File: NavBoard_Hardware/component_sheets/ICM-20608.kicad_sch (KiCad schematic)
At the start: 9 parts, among them U3 ICM-20608-G

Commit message: Updated sheet title info
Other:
- company: Missouri S&T Rover Design Team -> Thomas Francois, Katherine Dunlap, Missouri S&T Mars Rover Design Team
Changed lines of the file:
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@@
     (date "2022-09-15")
     (rev "2, 2023")
-    (company "Missouri S&T Rover Design Team")
+    (company "Thomas Francois, Katherine Dunlap, Missouri S&T Mars Rover Design Team")
     (comment 1 "ICM-2060B-G IMU & Supporting Components")
     (comment 2 "Provides Position & Acceleration Data")

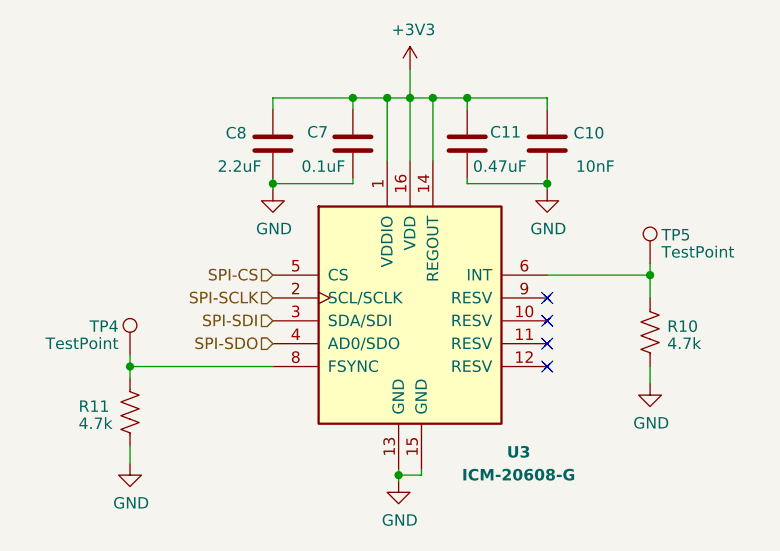
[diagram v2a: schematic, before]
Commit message: Corrected accelerometer regulator capacitors
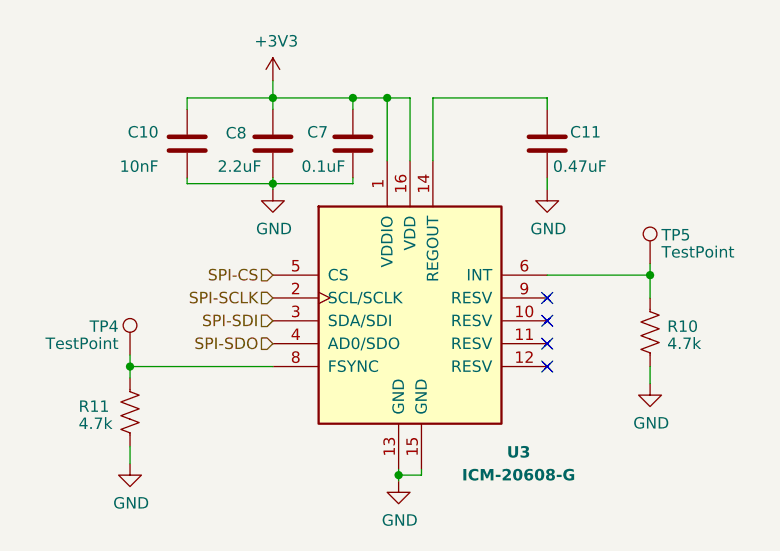
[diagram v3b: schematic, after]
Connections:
- net +3V3: no longer C11.1, U3.14 (REGOUT)
- new net: C11.1, U3.14 (REGOUT)
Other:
- moved on the sheet: C10, C11
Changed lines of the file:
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@@
   (junction (at 133.35 80.645) (diameter 0) (color 0 0 0 0)
   )
-  (junction (at 163.83 80.645) (diameter 0) (color 0 0 0 0)
-  )
-  (junction (at 148.59 71.12) (diameter 0) (color 0 0 0 0)
-  )
-  (junction (at 154.94 71.12) (diameter 0) (color 0 0 0 0)
+  (junction (at 133.35 71.12) (diameter 0) (color 0 0 0 0)
   )
   (junction (at 146.05 71.12) (diameter 0) (color 0 0 0 0)
-  )
-  (junction (at 151.13 71.12) (diameter 0) (color 0 0 0 0)
   )
   (no_connect (at 163.83 93.345))
@@
   (no_connect (at 163.83 98.425))
   (no_connect (at 163.83 100.965))
+  (wire (pts (xy 123.825 71.12) (xy 133.35 71.12))
+    (stroke (width 0) (type default) (color 0 0 0 0))
+  )
+  (wire (pts (xy 175.26 100.965) (xy 175.26 102.87))
+    (stroke (width 0) (type default) (color 0 0 0 0))
+  )
+  (wire (pts (xy 142.24 71.12) (xy 146.05 71.12))
+    (stroke (width 0) (type default) (color 0 0 0 0))
+  )
+  (wire (pts (xy 133.35 80.645) (xy 142.24 80.645))
+    (stroke (width 0) (type default) (color 0 0 0 0))
+  )
+  (wire (pts (xy 175.26 89.535) (xy 175.26 90.805))
+    (stroke (width 0) (type default) (color 0 0 0 0))
+  )
+  (wire (pts (xy 148.59 71.12) (xy 148.59 78.105))
+    (stroke (width 0) (type default) (color 0 0 0 0))
+  )
+  (wire (pts (xy 163.83 71.12) (xy 151.13 71.12))
+    (stroke (width 0) (type default) (color 0 0 0 0))
+  )
   (wire (pts (xy 133.35 71.12) (xy 142.24 71.12))
     (stroke (width 0) (type default) (color 0 0 0 0))
   )
+  (wire (pts (xy 123.825 72.39) (xy 123.825 71.12))
+    (stroke (width 0) (type default) (color 0 0 0 0))
+  )
+  (wire (pts (xy 117.475 109.855) (xy 117.475 111.76))
+    (stroke (width 0) (type default) (color 0 0 0 0))
+  )
+  (wire (pts (xy 147.32 113.03) (xy 147.32 113.665))
+    (stroke (width 0) (type default) (color 0 0 0 0))
+  )
+  (wire (pts (xy 117.475 100.965) (xy 133.35 100.965))
+    (stroke (width 0) (type default) (color 0 0 0 0))
+  )
   (wire (pts (xy 163.83 72.39) (xy 163.83 71.12))
     (stroke (width 0) (type default) (color 0 0 0 0))
   )
-  (wire (pts (xy 154.94 71.12) (xy 154.94 72.39))
-    (stroke (width 0) (type default) (color 0 0 0 0))
-  )
-  (wire (pts (xy 175.26 100.965) (xy 175.26 102.87))
-    (stroke (width 0) (type default) (color 0 0 0 0))
-  )
-  (wire (pts (xy 142.24 71.12) (xy 146.05 71.12))
-    (stroke (width 0) (type default) (color 0 0 0 0))
-  )
-  (wire (pts (xy 133.35 80.645) (xy 142.24 80.645))
-    (stroke (width 0) (type default) (color 0 0 0 0))
-  )
-  (wire (pts (xy 175.26 89.535) (xy 175.26 90.805))
-    (stroke (width 0) (type default) (color 0 0 0 0))
-  )
-  (wire (pts (xy 154.94 80.01) (xy 154.94 80.645))
-    (stroke (width 0) (type default) (color 0 0 0 0))
-  )
-  (wire (pts (xy 163.83 80.645) (xy 163.83 81.28))
-    (stroke (width 0) (type default) (color 0 0 0 0))
-  )
-  (wire (pts (xy 148.59 71.12) (xy 148.59 78.105))
-    (stroke (width 0) (type default) (color 0 0 0 0))
-  )
-  (wire (pts (xy 148.59 71.12) (xy 148.59 67.945))
-    (stroke (width 0) (type default) (color 0 0 0 0))
-  )
-  (wire (pts (xy 117.475 109.855) (xy 117.475 111.76))
-    (stroke (width 0) (type default) (color 0 0 0 0))
-  )
-  (wire (pts (xy 147.32 113.03) (xy 147.32 113.665))
-    (stroke (width 0) (type default) (color 0 0 0 0))
-  )
-  (wire (pts (xy 117.475 100.965) (xy 133.35 100.965))
-    (stroke (width 0) (type default) (color 0 0 0 0))
-  )
-  (wire (pts (xy 151.13 71.12) (xy 154.94 71.12))
-    (stroke (width 0) (type default) (color 0 0 0 0))
-  )
   (wire (pts (xy 149.86 112.395) (xy 149.86 113.03))
     (stroke (width 0) (type default) (color 0 0 0 0))
@@
     (stroke (width 0) (type default) (color 0 0 0 0))
   )
-  (wire (pts (xy 148.59 71.12) (xy 151.13 71.12))
-    (stroke (width 0) (type default) (color 0 0 0 0))
-  )
   (wire (pts (xy 142.24 71.12) (xy 142.24 72.39))
     (stroke (width 0) (type default) (color 0 0 0 0))
@@
     (stroke (width 0) (type default) (color 0 0 0 0))
   )
+  (wire (pts (xy 133.35 69.215) (xy 133.35 71.12))
+    (stroke (width 0) (type default) (color 0 0 0 0))
+  )
   (wire (pts (xy 117.475 99.695) (xy 117.475 100.965))
     (stroke (width 0) (type default) (color 0 0 0 0))
   )
-  (wire (pts (xy 154.94 80.645) (xy 163.83 80.645))
-    (stroke (width 0) (type default) (color 0 0 0 0))
-  )
   (wire (pts (xy 142.24 80.01) (xy 142.24 80.645))
     (stroke (width 0) (type default) (color 0 0 0 0))
@@
     (stroke (width 0) (type default) (color 0 0 0 0))
   )
+  (wire (pts (xy 123.825 80.645) (xy 123.825 80.01))
+    (stroke (width 0) (type default) (color 0 0 0 0))
+  )
+  (wire (pts (xy 133.35 80.645) (xy 123.825 80.645))
+    (stroke (width 0) (type default) (color 0 0 0 0))
+  )
   (wire (pts (xy 175.26 90.805) (xy 175.26 93.345))
     (stroke (width 0) (type default) (color 0 0 0 0))
   )
-  (wire (pts (xy 163.83 80.01) (xy 163.83 80.645))
-    (stroke (width 0) (type default) (color 0 0 0 0))
-  )
-  (wire (pts (xy 154.94 71.12) (xy 163.83 71.12))
-    (stroke (width 0) (type default) (color 0 0 0 0))
-  )
   (wire (pts (xy 133.35 72.39) (xy 133.35 71.12))
+    (stroke (width 0) (type default) (color 0 0 0 0))
+  )
+  (wire (pts (xy 163.83 80.01) (xy 163.83 81.28))
     (stroke (width 0) (type default) (color 0 0 0 0))
   )
@@
     (pin "1")
   )
-  (symbol (lib_id "Device:C") (at 163.83 76.2 0) (unit 1)
-    (in_bom yes) (on_board yes)
-    (property "Reference" "C10" (id 0) (at 166.751 75.0316 0)
-      (effects (font (size 1.27 1.27)) (justify left))
-    )
-    (property "Value" "10nF" (id 1) (at 167.005 78.74 0)
-      (effects (font (size 1.27 1.27)) (justify left))
-    )
-    (property "Footprint" "Capacitor_SMD:C_0603_1608Metric_Pad1.08x0.95mm_HandSolder" (id 2) (at 164.7952 80.01 0)
-      (effects (font (size 1.27 1.27)) hide)
-    )
-    (property "Datasheet" "~" (id 3) (at 163.83 76.2 0)
+  (symbol (lib_id "Device:C") (at 123.825 76.2 0) (mirror y) (unit 1)
+    (in_bom yes) (on_board yes)
+    (property "Reference" "C10" (id 0) (at 120.65 74.93 0)
+      (effects (font (size 1.27 1.27)) (justify left))
+    )
+    (property "Value" "10nF" (id 1) (at 120.65 78.74 0)
+      (effects (font (size 1.27 1.27)) (justify left))
+    )
+    (property "Footprint" "Capacitor_SMD:C_0603_1608Metric_Pad1.08x0.95mm_HandSolder" (id 2) (at 122.8598 80.01 0)
+      (effects (font (size 1.27 1.27)) hide)
+    )
+    (property "Datasheet" "~" (id 3) (at 123.825 76.2 0)
       (effects (font (size 1.27 1.27)) hide)
     )
@@
     (pin "1")
   )
-  (symbol (lib_id "Device:C") (at 154.94 76.2 0) (unit 1)
-    (in_bom yes) (on_board yes)
-    (property "Reference" "C11" (id 0) (at 157.48 74.93 0)
-      (effects (font (size 1.27 1.27)) (justify left))
-    )
-    (property "Value" "0.47uF" (id 1) (at 155.575 78.74 0)
-      (effects (font (size 1.27 1.27)) (justify left))
-    )
-    (property "Footprint" "Capacitor_SMD:C_0603_1608Metric_Pad1.08x0.95mm_HandSolder" (id 2) (at 155.9052 80.01 0)
-      (effects (font (size 1.27 1.27)) hide)
-    )
-    (property "Datasheet" "~" (id 3) (at 154.94 76.2 0)
+  (symbol (lib_id "Device:C") (at 163.83 76.2 0) (unit 1)
+    (in_bom yes) (on_board yes)
+    (property "Reference" "C11" (id 0) (at 166.37 74.93 0)
+      (effects (font (size 1.27 1.27)) (justify left))
+    )
+    (property "Value" "0.47uF" (id 1) (at 164.465 78.74 0)
+      (effects (font (size 1.27 1.27)) (justify left))
+    )
+    (property "Footprint" "Capacitor_SMD:C_0603_1608Metric_Pad1.08x0.95mm_HandSolder" (id 2) (at 164.7952 80.01 0)
+      (effects (font (size 1.27 1.27)) hide)
+    )
+    (property "Datasheet" "~" (id 3) (at 163.83 76.2 0)
       (effects (font (size 1.27 1.27)) hide)
     )
@@
     (pin "9")
   )
-  (symbol (lib_id "power:+3V3") (at 148.59 67.945 0) (unit 1)
-    (in_bom yes) (on_board yes)
-    (property "Reference" "#PWR0103" (id 0) (at 148.59 71.755 0)
-      (effects (font (size 1.27 1.27)) hide)
-    )
-    (property "Value" "+3V3" (id 1) (at 148.971 63.5508 0))
-    (property "Footprint" "" (id 2) (at 148.59 67.945 0)
-      (effects (font (size 1.27 1.27)) hide)
-    )
-    (property "Datasheet" "" (id 3) (at 148.59 67.945 0)
-      (effects (font (size 1.27 1.27)) hide)
-    )
+  (symbol (lib_id "power:+3V3") (at 133.35 69.215 0) (unit 1)
+    (in_bom yes) (on_board yes)
+    (property "Reference" "#PWR0103" (id 0) (at 133.35 73.025 0)
+      (effects (font (size 1.27 1.27)) hide)
+    )
+    (property "Value" "+3V3" (id 1) (at 133.731 64.8208 0))
+    (property "Footprint" "" (id 2) (at 133.35 69.215 0)
+      (effects (font (size 1.27 1.27)) hide)
+    )
+    (property "Datasheet" "" (id 3) (at 133.35 69.215 0)
+      (effects (font (size 1.27 1.27)) hide)
+    )
